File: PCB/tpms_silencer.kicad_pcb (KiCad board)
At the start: 2 copper layers, 33 x 51.6 mm, 24 parts, among them J1 AVR-ISP-6, U1 ATtiny841-SSU, U2 MICRF112, Y1 8MHz, Y2 9.84375MHz

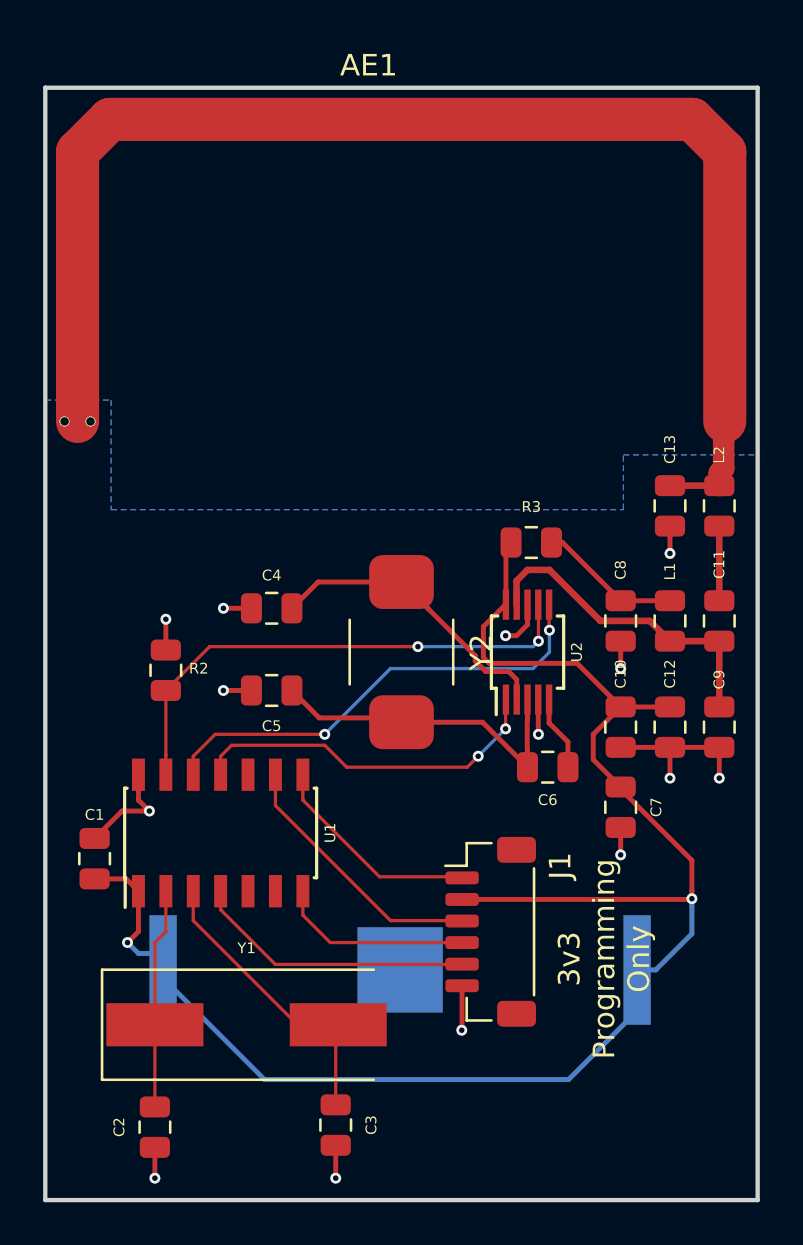
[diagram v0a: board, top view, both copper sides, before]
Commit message: Change programming header, comments on capacitor, v2 layout, hole for mounting in enclosure
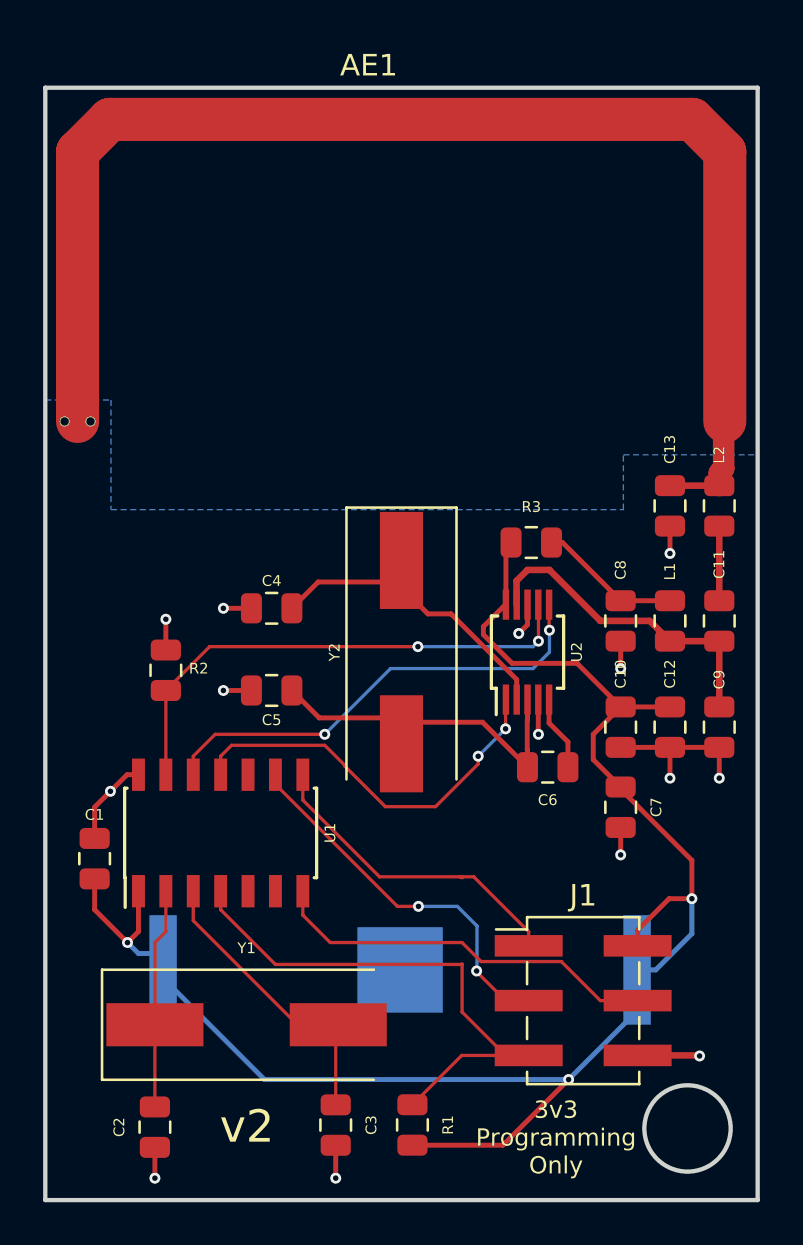
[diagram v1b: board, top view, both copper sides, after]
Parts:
- added R1: 100k, Resistor_SMD:R_0805_2012Metric, F.Cu at (39.9, 70.9)
- C6: value 3.3pF -> 10pF
- J1: footprint Connector_JST:JST_SH_BM06B-SRSS-TB_1x06-1MP_P1.00mm_Vertical -> Connector_PinHeader_2.54mm:PinHeader_2x03_P2.54mm_Vertical_SMD
- U2: value MICRF112 -> MICRF112YMM
- Y2: footprint Crystal:Crystal_SMD_TXC_AX_8045-2Pin_8.0x4.5mm -> Crystal:Crystal_SMD_HC49-SD
- moved J1 5.35 mm to (47.8, 65.2), turned to 0 degrees
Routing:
- net /RST: track 13.0 -> 25.5 mm
- net /MOSI: track 8.92 -> 18.2 mm
- net /SCK: track 12.1 -> 17.7 mm, vias 0 -> 2
- net /MISO: track 10.1 -> 15.0 mm
- net VDD: track 76.1 -> 78.6 mm, vias 2 -> 3
- net /ASK: track 16.4 -> 18.2 mm
- net Net-(C4-Pad1): track 13.9 -> 14.9 mm
- net GNDREF: track 29.4 -> 28.7 mm
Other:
- outline, holes or cut-outs redrawn
- board text added: "v2"

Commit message: V2 - sent for fab.
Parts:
- added SW1: SW_SPST, Button_Switch_SMD:SW_SPST_PTS645, F.Cu at (39.3, 63.7)
- J1: footprint Connector_PinHeader_2.54mm:PinHeader_2x03_P2.54mm_Vertical_SMD -> !Custom:AVR-SMD-Programming-Header; moved to B.Cu
- Y1: footprint Crystal:Crystal_SMD_HC49-SD -> Crystal:Crystal_SMD_TXC_7A-2Pin_5x3.2mm
- moved J1 24.9 mm to (30.0, 47.8)
- moved C3 5.48 mm to (31.0, 69.7)
- moved Y1 3.25 mm to (29.0, 65.5)
- moved C1 2.13 mm to (25.1, 56.5)
- moved R2 2.03 mm to (28.4, 47.8)
- moved C4 1.78 mm to (35.1, 47.0)
- moved C5 1.78 mm to (35.1, 50.8)
- moved C2 1.57 mm to (27.2, 69.7)
- moved U1 1.11 mm to (31.0, 56.3)
- moved Y2 0.77 mm to (40.1, 49.1)
- moved C6 0.43 mm to (45.8, 54.6)
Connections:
- U1 pad 6: (no net) -> Net-(SW1-Pad1)
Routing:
- net VDD: track 78.6 -> 94.0 mm, vias 3 -> 4
- net /RST: track 25.5 -> 34.7 mm, vias 0 -> 1
- net /FSK: track 21.4 -> 29.2 mm
- net /SCK: track 17.7 -> 13.0 mm, vias 2 -> 1
- net /MISO: track 15.0 -> 11.2 mm, vias 0 -> 1
- net Net-(C3-Pad1): track 13.8 -> 10.3 mm
- net Net-(SW1-Pad1): track 0.00 -> 3.30 mm
- net GNDREF: track 28.7 -> 31.8 mm, vias 14 -> 13
- net /MOSI: track 18.2 -> 15.7 mm, vias 0 -> 1
- net /EN: track 23.6 -> 25.2 mm
- net Net-(C4-Pad1): track 14.9 -> 13.8 mm
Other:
- outline, holes or cut-outs redrawn
- net class Antenna: via_dia 0.508 -> 0.74
- net class Default: via_dia 0.508 -> 0.6; via_drill 0.254 -> 0.3
- net class Large: via_dia 0.508 -> 0.6; via_drill 0.254 -> 0.3
- net class Medium: via_dia 0.508 -> 0.6; via_drill 0.254 -> 0.3
- rule via_min_drill: 0.254 -> 0.3
- rule via_min_size: 0.508 -> 0.6
- board text added: "TPMS Silencer v2"
- board text removed: "v2"

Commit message: Prep for release.
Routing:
- net GNDREF: track 31.8 -> 39.7 mm
- net Net-(SW1-Pad1): track 3.30 -> 11.3 mm
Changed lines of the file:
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@@
-(kicad_pcb (version 20171130) (host pcbnew "(5.0.1)-rc2")
+(kicad_pcb (version 20171130) (host pcbnew "(5.1.0)-1")
   (general
     (thickness 1.6)
     (drawings 7)
-    (tracks 189)
+    (tracks 191)
     (zones 0)
     (modules 26)
@@
     (zone_45_only no)
     (trace_min 0.1524)
-    (segment_width 0.2)
-    (edge_width 0.2)
     (via_size 0.6)
     (via_drill 0.3)
@@
     (uvia_min_size 0.2)
     (uvia_min_drill 0.1)
+    (edge_width 0.2)
+    (segment_width 0.2)
     (pcb_text_width 0.3)
     (pcb_text_size 1.5 1.5)
@@
     (solder_mask_min_width 0.25)
     (aux_axis_origin 0 0)
-    (visible_elements 7FFFFFFF)
+    (visible_elements 7FFFEFFF)
     (pcbplotparams
       (layerselection 0x010fc_ffffffff)
@@
     (uvia_dia 0.508)
     (uvia_drill 0.254)
+    (diff_pair_width 0.1524)
     (diff_pair_gap 0.1524)
-    (diff_pair_width 0.1524)
     (add_net /ASK)
     (add_net /EN)
@@
     (uvia_dia 0.508)
     (uvia_drill 0.254)
+    (diff_pair_width 0.1524)
     (diff_pair_gap 0.1524)
-    (diff_pair_width 0.1524)
   )
   (net_class Large ""
@@
     (uvia_dia 0.508)
     (uvia_drill 0.254)
+    (diff_pair_width 0.1524)
     (diff_pair_gap 0.1524)
-    (diff_pair_width 0.1524)
     (add_net "Net-(AE1-Pad1)")
     (add_net "Net-(C11-Pad1)")
@@
     (uvia_dia 0.508)
     (uvia_drill 0.254)
+    (diff_pair_width 0.1524)
     (diff_pair_gap 0.1524)
-    (diff_pair_width 0.1524)
     (add_net GNDREF)
     (add_net "Net-(C4-Pad1)")
@@
   (segment (start 45.212 48.26) (end 44.958 48.514) (width 0.2286) (layer Top) (net 2))
   (segment (start 45.212 46.822) (end 45.212 48.26) (width 0.2286) (layer Top) (net 2))
+  (segment (start 35.306 65.9892) (end 43.266 65.9892) (width 0.2286) (layer Top) (net 2))
   (segment (start 28.448 58.994) (end 28.448 62.738) (width 0.1524) (layer Top) (net 3) (status 10))
   (segment (start 27.178 64.008) (end 27.178 65.532) (width 0.1524) (layer Top) (net 3) (status 20))
@@
   (segment (start 33.528 59.8362) (end 35.181 61.4892) (width 0.1524) (layer Top) (net 19) (status 20))
   (segment (start 33.528 58.994) (end 33.528 59.8362) (width 0.1524) (layer Top) (net 19) (status 10))
+  (segment (start 35.306 61.4892) (end 43.266 61.4892) (width 0.1524) (layer Top) (net 19))
   (zone (net 2) (net_name GNDREF) (layer Bottom) (hatch edge 0.508)
     (connect_pads (clearance 0.508))

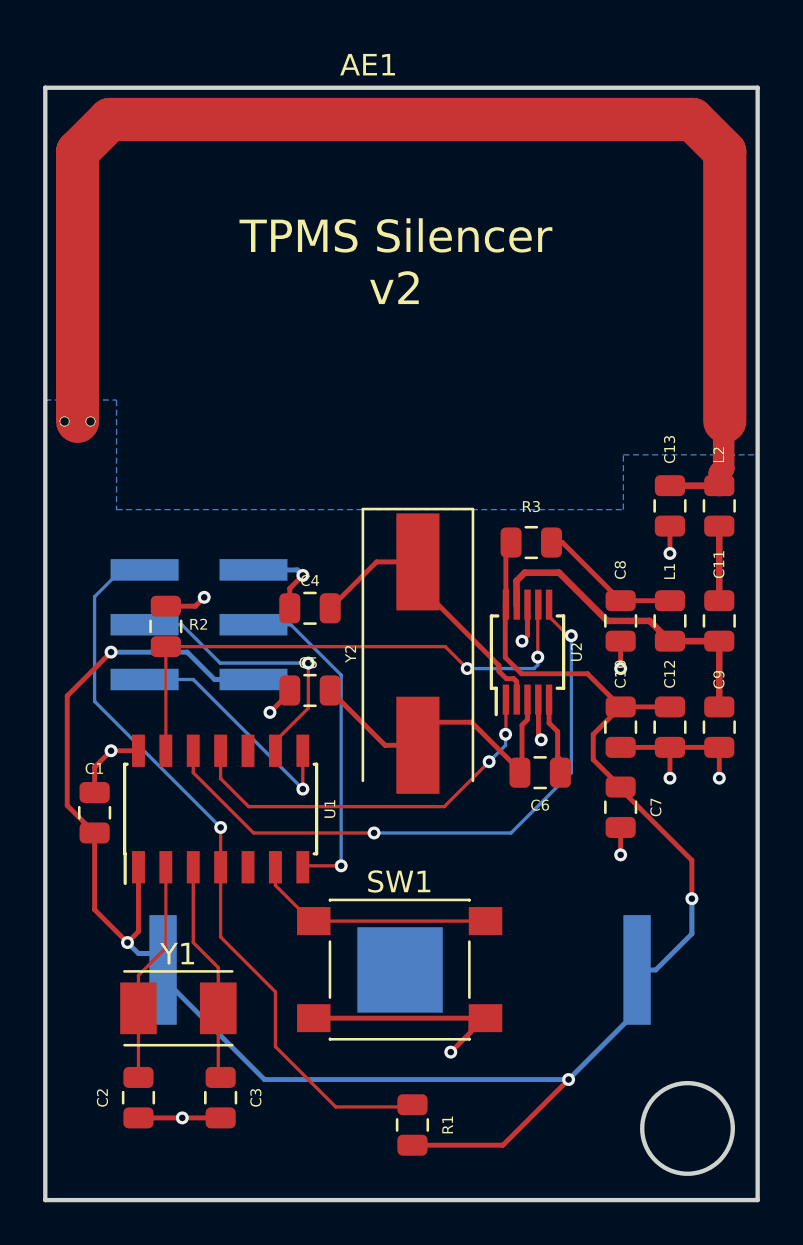
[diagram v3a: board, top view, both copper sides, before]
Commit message: add test points and update annotation to match MICRF112-315-EV
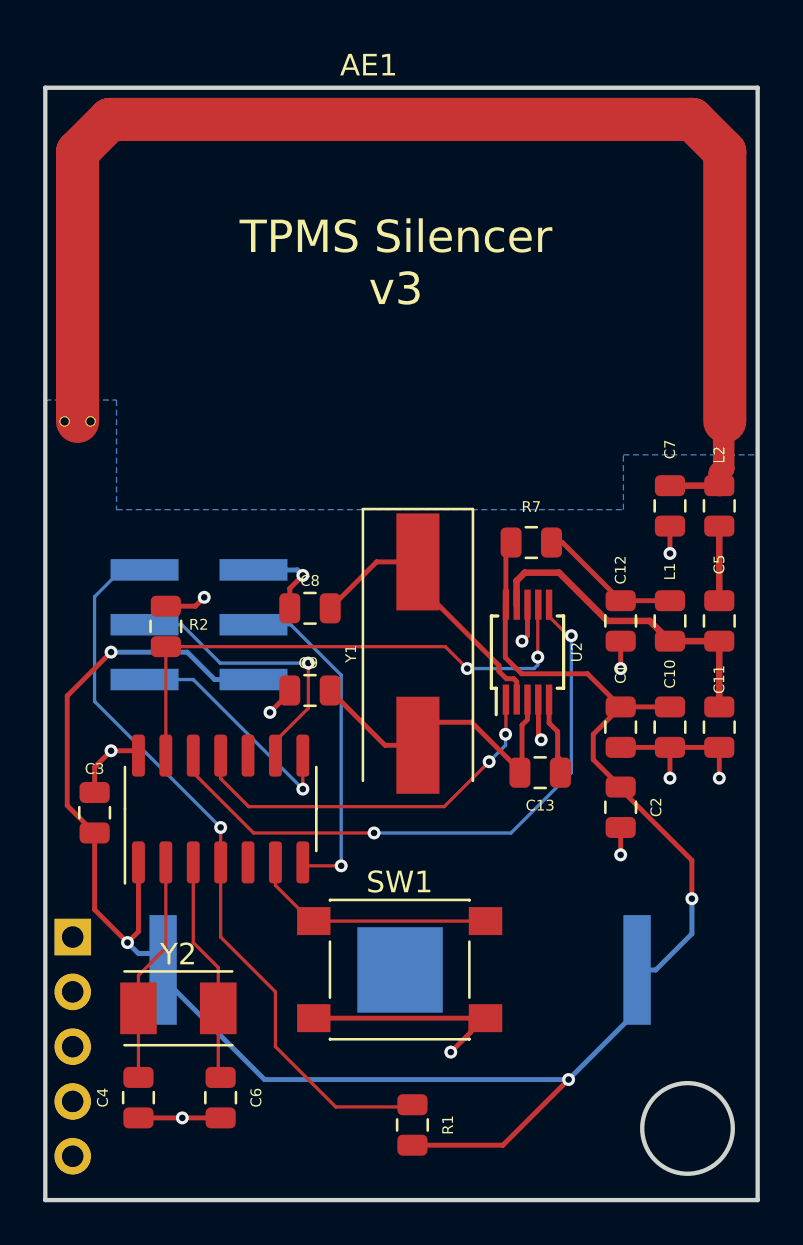
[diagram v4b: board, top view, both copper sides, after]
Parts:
- added J2: TEST, Connector_PinHeader_2.54mm:PinHeader_1x05_P2.54mm_Horizontal, B.Cu at (24.1, 62.2)
- U1: value ATtiny841-SSU -> ATtiny841-SS
- renumbered C10 to C1, C12 to C10, C9 to C11, C8 to C12, C6 to C13, C7 to C2, C1 to C3, C2 to C4, C11 to C5, C3 to C6, C13 to C7, C4 to C8, C5 to C9, R3 to R7, Y2 to Y1, Y1 to Y2
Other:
- board text added: "+V"
- board text added: "ASK"
- board text added: "EN"
- board text added: "FSK"
- board text added: "GND"
- board text added: "TPMS Silencer v3"
- board text removed: "TPMS Silencer v2"

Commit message: update to kicad v6
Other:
- net class Antenna removed
- net class Default removed
- net class Large removed
- net class Medium removed
